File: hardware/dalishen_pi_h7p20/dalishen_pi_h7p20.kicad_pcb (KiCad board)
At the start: 4 copper layers, 92 x 64 mm, 238 parts, among them J1 Conn_02x05_Odd_Even, J10 RJ45_HR911130A, J1001 USB_C_Receptacle_USB2.0_16P, J2 USB_C_Receptacle_USB2.0_16P, J3 USB_A, J6 5V, J7 OV5640, J9 D500C930SV0, SW1 SW_Push, SW2 SW_Push, SW3 SW_DIP_x03, SW4 SW_Push, SW5 SW_Push, U1 YT8531C, U1001 AIC8800FC, U1002 P25Q80H/P25Q64H/P25Q128HA, U18 LM2903A-VR, U19 LM2903A-VR, U2 LM2903A-VR, U20 USB3343, U3 H7P20N0L128-M3H1, U4 SY7201ABC, U5 XC6206-2.8, U6 EA3036C, U7 P25Q64SH-SSH-IR, U8 XC6206-1.5, U9 CJ3439KDW, X1 NC, Y1 26M, Y1001 26M, 10PPM, Y2 NC

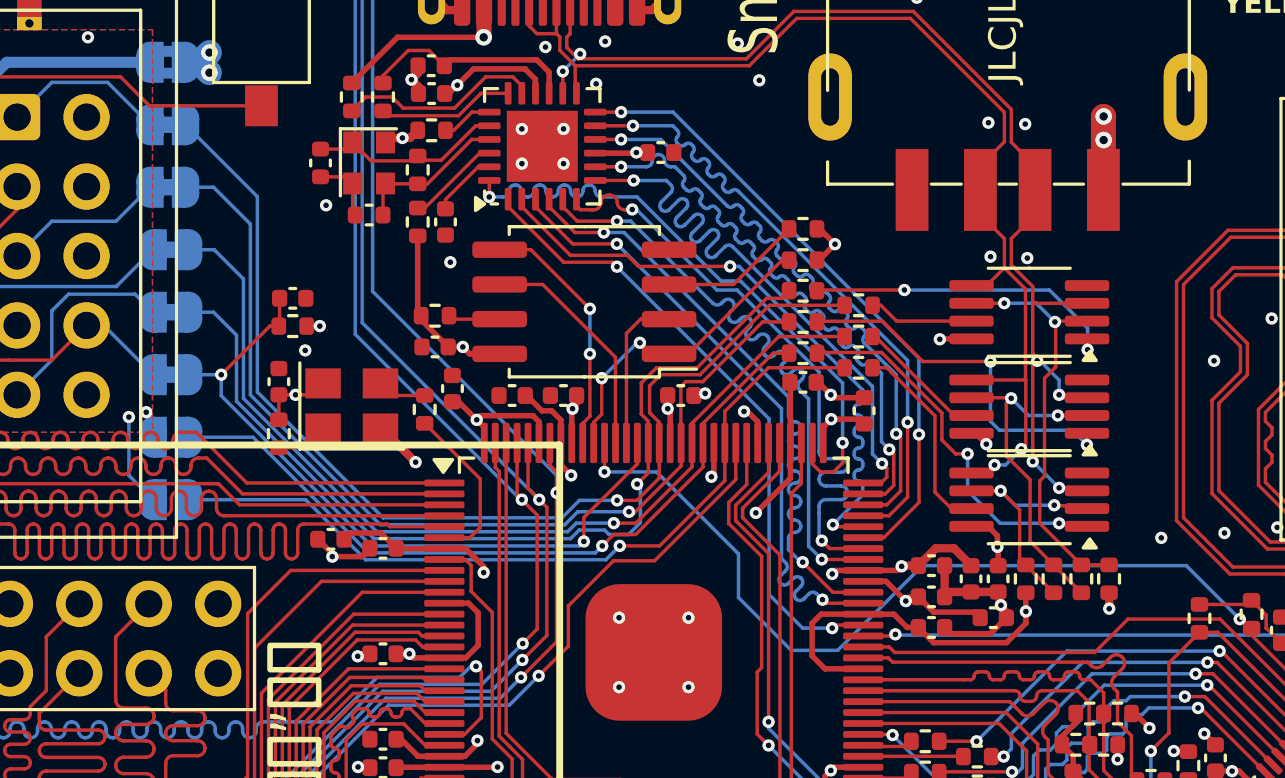
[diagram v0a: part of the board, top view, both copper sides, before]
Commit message: [dalishen_pi_h7p20] 由于JTAG口在LQFP128封装上无法作为IO使用，故移除SE0，J, K状态电路
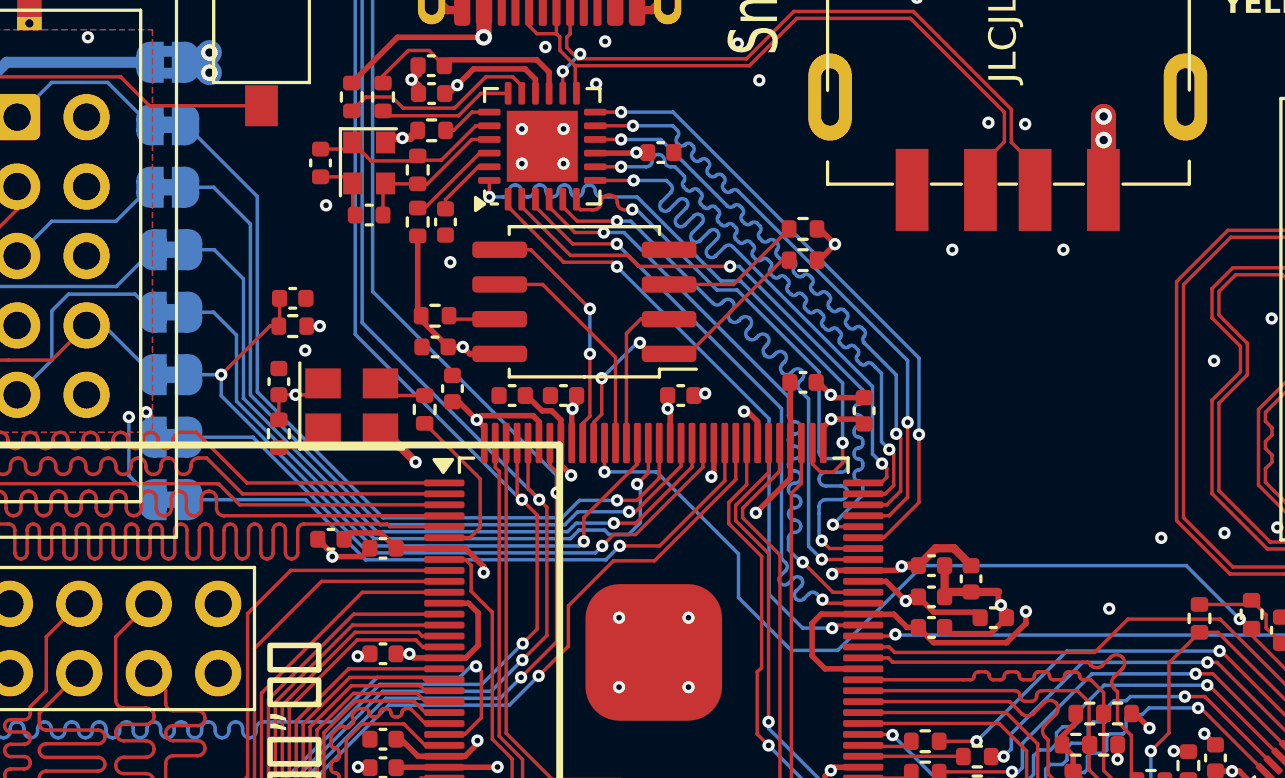
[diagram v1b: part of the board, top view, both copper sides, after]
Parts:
- removed C1: 0.1uF, Capacitor_SMD:C_0402_1005Metric
- removed JP1, JP10: SolderJumper_2_Open, Jumper:SolderJumper-2_P1.3mm_Open_RoundedPad1.0x1.5mm
- removed R1: 10k,1%, Resistor_SMD:R_0402_1005Metric
- removed R10, R3: 4.7k, Resistor_SMD:R_0402_1005Metric
- removed R2: 33k, Resistor_SMD:R_0402_1005Metric
- removed R23, R24, R25, R26, R27, R28: 2.49k, Resistor_SMD:R_0402_1005Metric
- removed U18, U19, U2: LM2903A-VR, Package_SO:MSOP-8_3x3mm_P0.65mm
- added JP7: SolderJumper_2_Bridged, Jumper:SolderJumper-2_P1.3mm_Bridged_RoundedPad1.0x1.5mm, B.Cu at (138.5, 112.8)
- added JP8: SolderJumper_2_Bridged, Jumper:SolderJumper-2_P1.3mm_Bridged_RoundedPad1.0x1.5mm, B.Cu at (138.5, 115.1)
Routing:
- net /VCC_5V: track 235.1 -> 195.5 mm, vias 14 -> 11
- net /USB334x/USB20_D_N: track 45.4 -> 27.5 mm, vias 6 -> 2
- net /USB334x/USB20_D_P: track 41.9 -> 26.1 mm, vias 2 -> 0
- net /USB334x/CMP_REF_1: track 15.3 -> 0.00 mm, vias 2 -> 0
- net /USB20_DM_CMP3: track 13.9 -> 0.00 mm, vias 2 -> 0
- net /USB20_DM_CMP2: track 13.5 -> 0.00 mm, vias 2 -> 0
- net /USB334x/CMP_REF_2: track 12.8 -> 0.00 mm, vias 2 -> 0
- net /USB20_DM_CMP1: track 11.7 -> 0.00 mm, vias 2 -> 0
- net /FPGA_TCK: track 40.0 -> 29.4 mm
- net /FPGA_TDI: track 34.0 -> 24.9 mm
- net /USB334x/CMP_REF_3: track 8.98 -> 0.00 mm, vias 2 -> 0
- net /FPGA_TDO: track 34.7 -> 27.1 mm
- net /USB20_DP_CMP3: track 7.39 -> 0.00 mm
- net /FPGA_TMS: track 35.7 -> 28.7 mm
- net /FPGA_TX: track 29.3 -> 23.1 mm
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
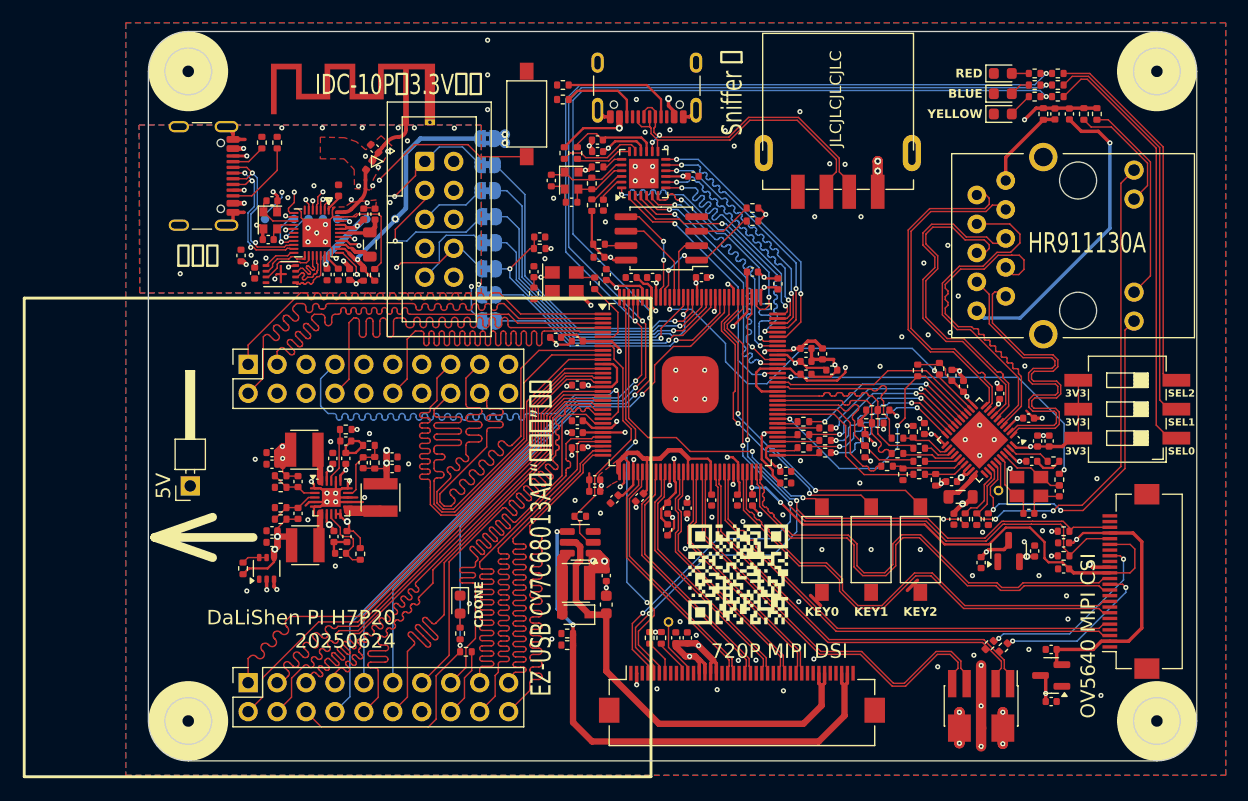
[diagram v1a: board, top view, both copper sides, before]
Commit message: [dalishen_pi_h7p20] production_files.20250711 不贴片，仅用于电源排查
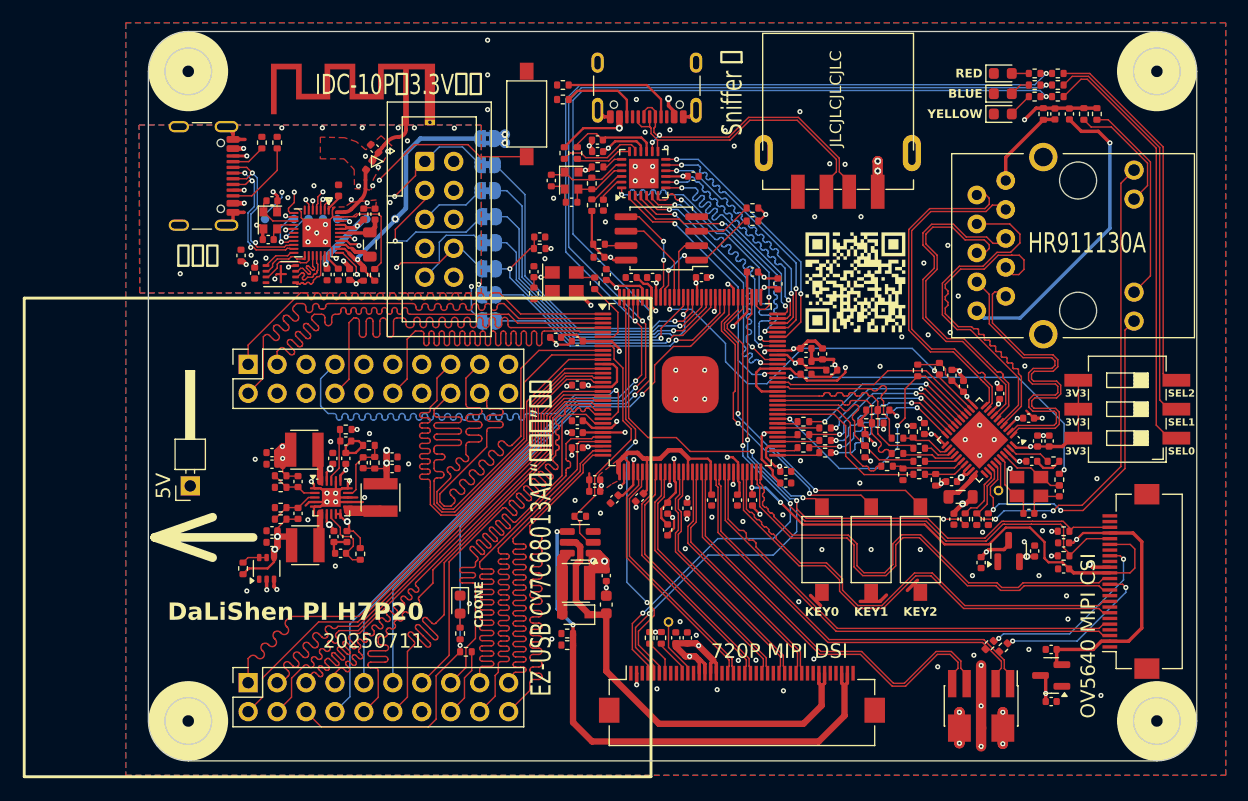
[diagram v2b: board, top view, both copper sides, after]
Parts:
- moved G*** 27.6 mm to (170.7, 111.7)
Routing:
- net GND: track 108.3 -> 110.8 mm
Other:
- board text added: "20250711"
- board text added: "DaLiShen PI H7P20"
- board text removed: "DaLiShen PI H7P20 20250624"

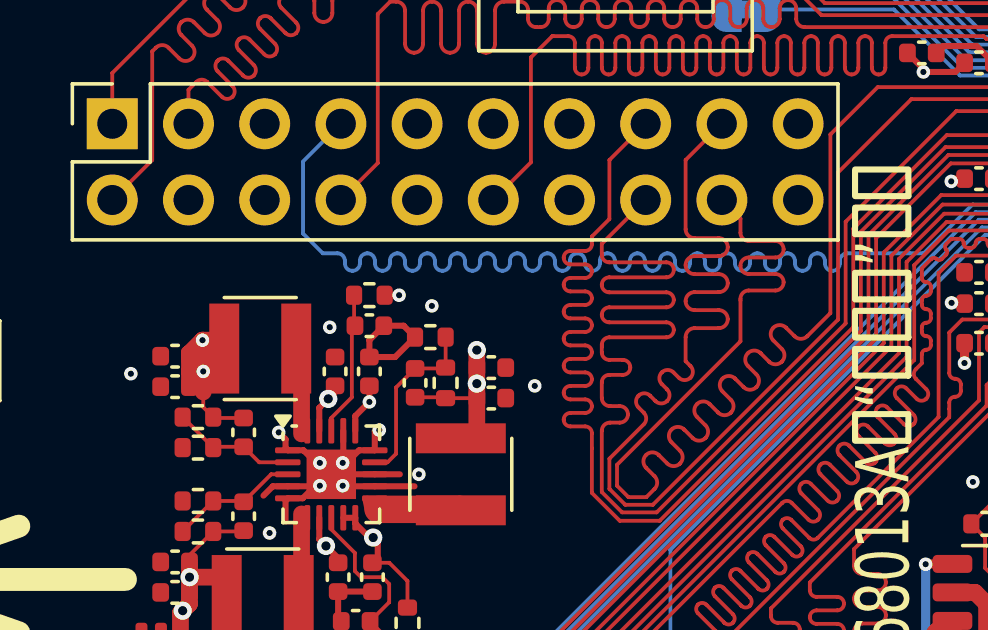
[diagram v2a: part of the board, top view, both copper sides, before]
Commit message: [dalishen_pi_h7p20] 两个双排针的VCC脚通过短接点连接3.3V，预留给其他扩展模块供电的能力。
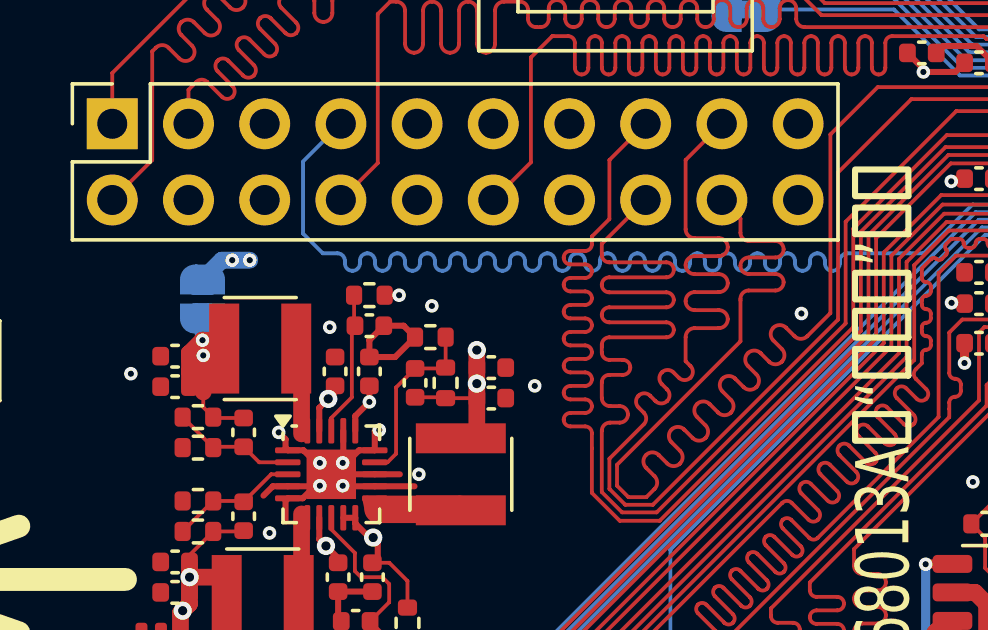
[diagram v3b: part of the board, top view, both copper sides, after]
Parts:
- added JP1: SolderJumper_2_Open, Jumper:SolderJumper-2_P1.3mm_Open_RoundedPad1.0x1.5mm, B.Cu at (120.4, 124.7)
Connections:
- CY_J1 pad 10: unconnected-(CY_J1-Pin_10-Pad10) -> Net-(CY_J1-Pin_10)
- CY_J1 pad 20: unconnected-(CY_J1-Pin_20-Pad20) -> Net-(CY_J1-Pin_10)
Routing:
- net Net-(CY_J1-Pin_10): track 0.00 -> 23.5 mm, vias 0 -> 2
- net /VCC_3V3: track 122.1 -> 123.3 mm
- net /VDD_CORE: track 76.7 -> 77.8 mm
- net GND: vias 151 -> 152
